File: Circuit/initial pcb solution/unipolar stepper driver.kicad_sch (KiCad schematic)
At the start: 21 parts, among them Q1 S8050, Q2 S8050, Q3 S8050, Q4 S8050

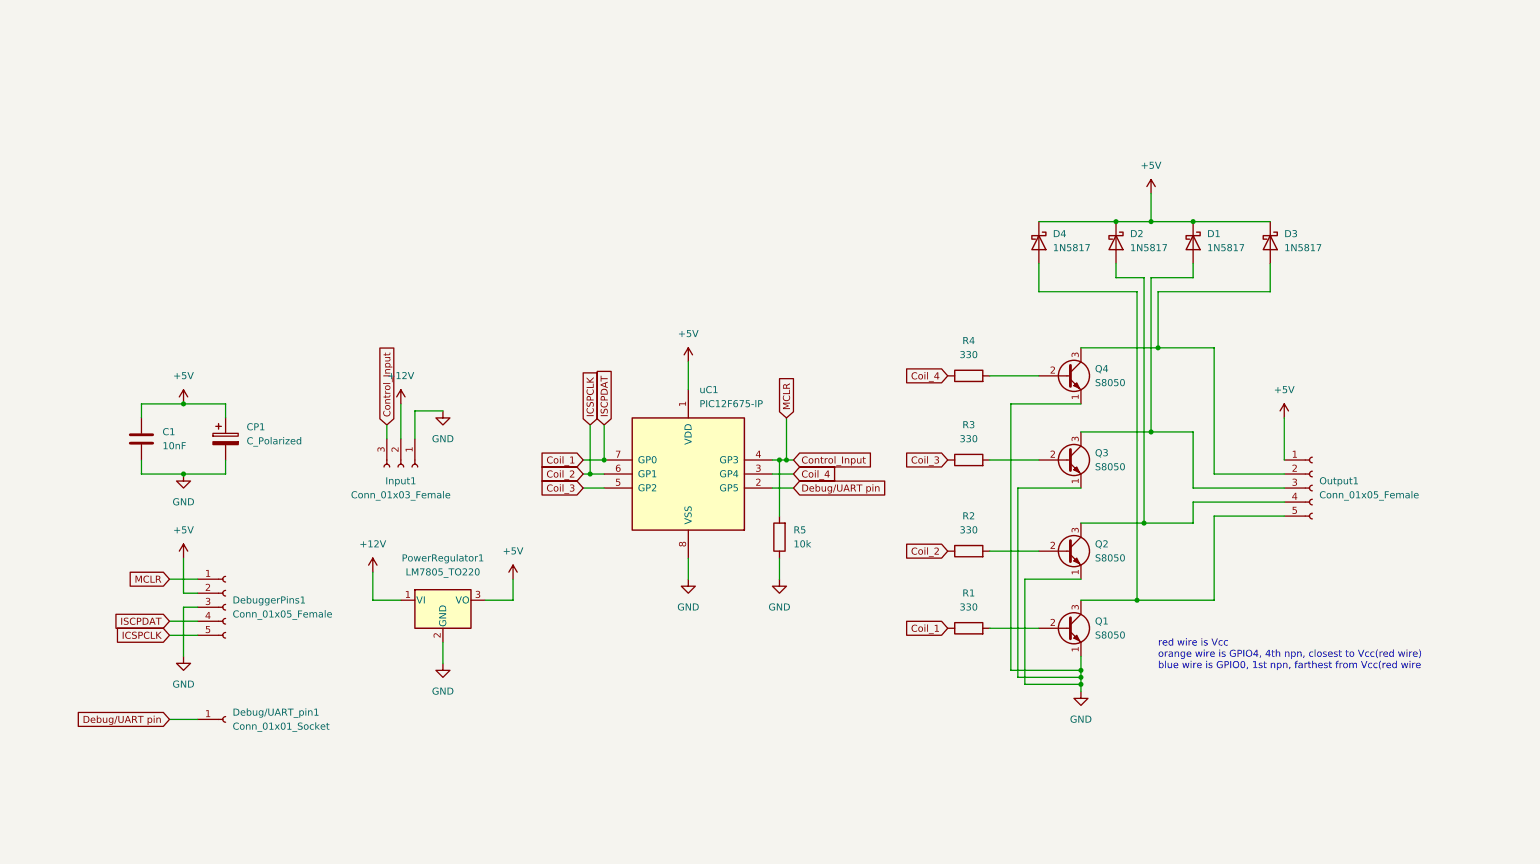
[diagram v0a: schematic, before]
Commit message: Developed V2 Circuit schematic AND PCB
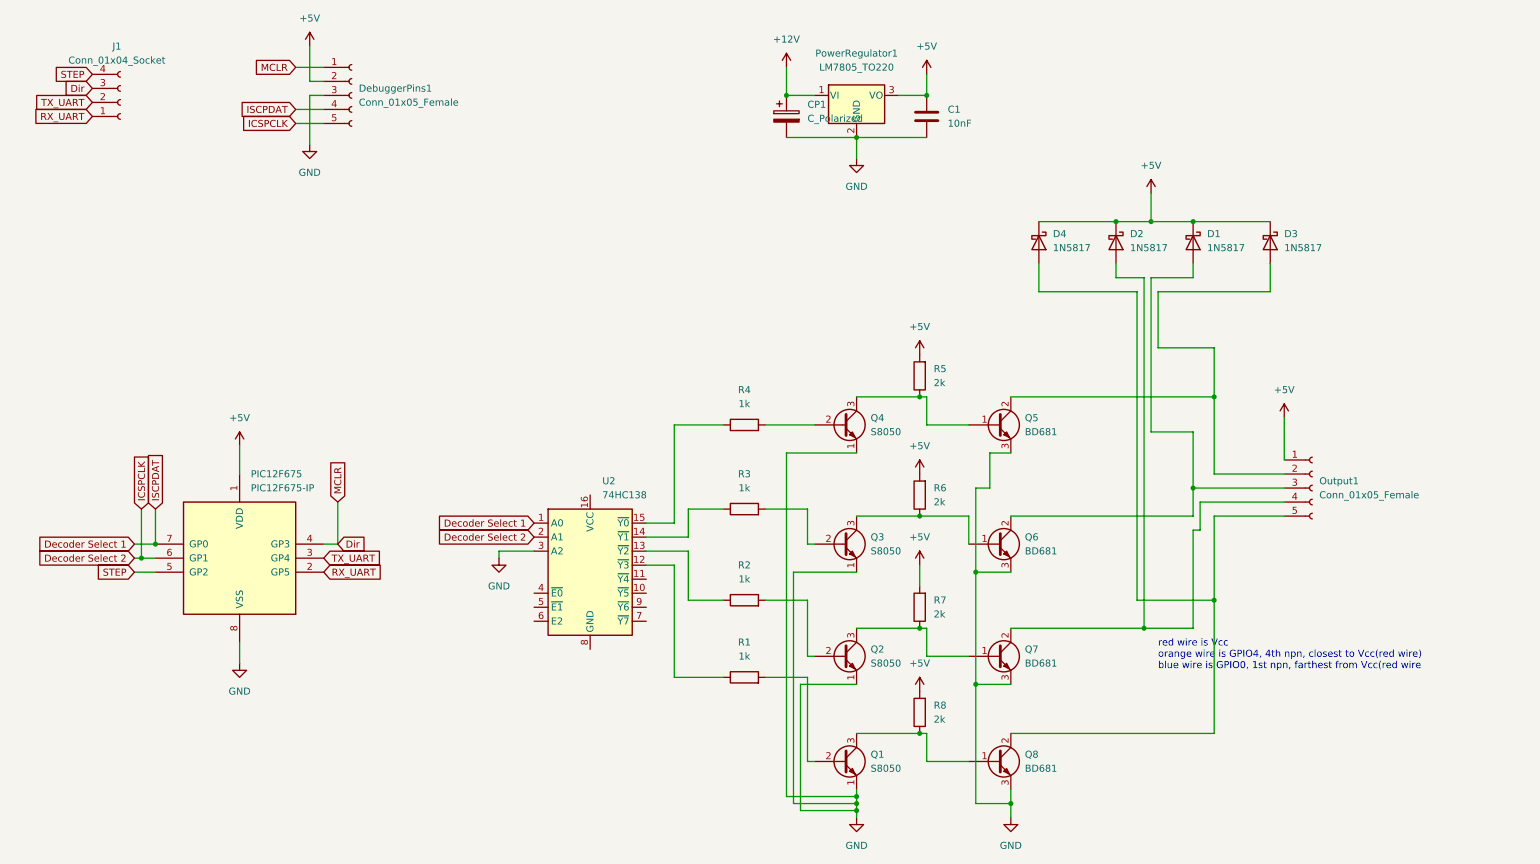
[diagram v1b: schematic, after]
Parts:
- removed Debug/UART_pin1: Conn_01x01_Socket, Connector_PinSocket_2.54mm:PinSocket_1x01_P2.54mm_Vertical, symbol Connector:Conn_01x01_Socket
- removed Input1: Conn_01x03_Female, Connector_PinHeader_2.54mm:PinHeader_1x03_P2.54mm_Vertical, symbol Connector:Conn_01x03_Female
- added J1: Conn_01x04_Socket, Connector_PinSocket_2.54mm:PinSocket_1x04_P2.54mm_Vertical, symbol Connector:Conn_01x04_Socket
- added Q5, Q6, Q7, Q8: BD681, Package_TO_SOT_THT:TO-126-3_Vertical, symbol Device:Q_NPN_BCE
- added R6, R7, R8: 2k, Resistor_THT:R_Axial_DIN0207_L6.3mm_D2.5mm_P10.16mm_Horizontal, symbol Device:R
- added U2: 74HC138, Package_DIP:DIP-16_W7.62mm_LongPads, symbol 74xx:74HC138
- R1, R2, R3, R4: value 330 -> 1k
- R5: value 10k -> 2k; footprint Resistor_THT:R_Axial_DIN0207_L6.3mm_D2.5mm_P7.62mm_Horizontal -> Resistor_THT:R_Axial_DIN0207_L6.3mm_D2.5mm_P10.16mm_Horizontal
- renumbered uC1 to PIC12F675
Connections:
- net +12V: now also CP1.1
- net +5V: now also R5.2, R6.2, R7.2, R8.2; no longer CP1.1
- net GND: now also Q5.3 (E), Q6.3 (E), Q7.3 (E), Q8.3 (E), U2.3 (A2); no longer R5.1
- net at D1.2 (A), Output1.3 (Pin_3): now also Q6.2 (C); no longer Q3.3 (C)
- net at D4.2 (A), Output1.5 (Pin_5): now also Q8.2 (C); no longer Q1.3 (C)
- net at D3.2 (A), Output1.2 (Pin_2): now also Q5.2 (C); no longer Q4.3 (C)
- net at D2.2 (A), Output1.4 (Pin_4): now also Q7.2 (C); no longer Q2.3 (C)
- net Coil_1 renamed Decoder Select 1
- net Decoder Select 1: now also U2.1 (A0); no longer R1.1
- net Coil_2 renamed Decoder Select 2
- net Decoder Select 2: now also U2.2 (A1); no longer R2.1
- net Coil_3: no longer names the net of R3.1
- net Coil_3: now also U2.14 (~{Y1}); no longer PIC12F675.5 (GP2)
- net Coil_4: no longer names the net of R4.1
- net Coil_4: now also U2.15 (~{Y0}); no longer PIC12F675.3 (GP4)
- net Control_Input renamed Dir
- net Dir: now also J1.3 (Pin_3); no longer R5.2
- net Debug/UART pin renamed RX_UART
- net RX_UART: now also J1.1 (Pin_1)
- new net: R1.1, U2.12 (~{Y3})
- new net: R2.1, U2.13 (~{Y2})
- new net: Q4.3 (C), Q5.1 (B), R5.1
- new net: Q1.3 (C), Q8.1 (B), R8.1
- new net: Q2.3 (C), Q7.1 (B), R7.1
- new net: Q3.3 (C), Q6.1 (B), R6.1
- new net STEP: J1.4 (Pin_4), PIC12F675.5 (GP2)
- new net TX_UART: J1.2 (Pin_2), PIC12F675.3 (GP4)
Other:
- moved on the sheet: C1, CP1, DebuggerPins1, PIC12F675, PowerRegulator1, Q1, Q2, Q3, Q4, R1, R2, R3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
